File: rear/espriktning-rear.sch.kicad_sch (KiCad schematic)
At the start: 26 parts, among them J1 USB_C_Receptacle_USB2.0, J4 Conn_01x08, SW1 Reset, SW2 Flash

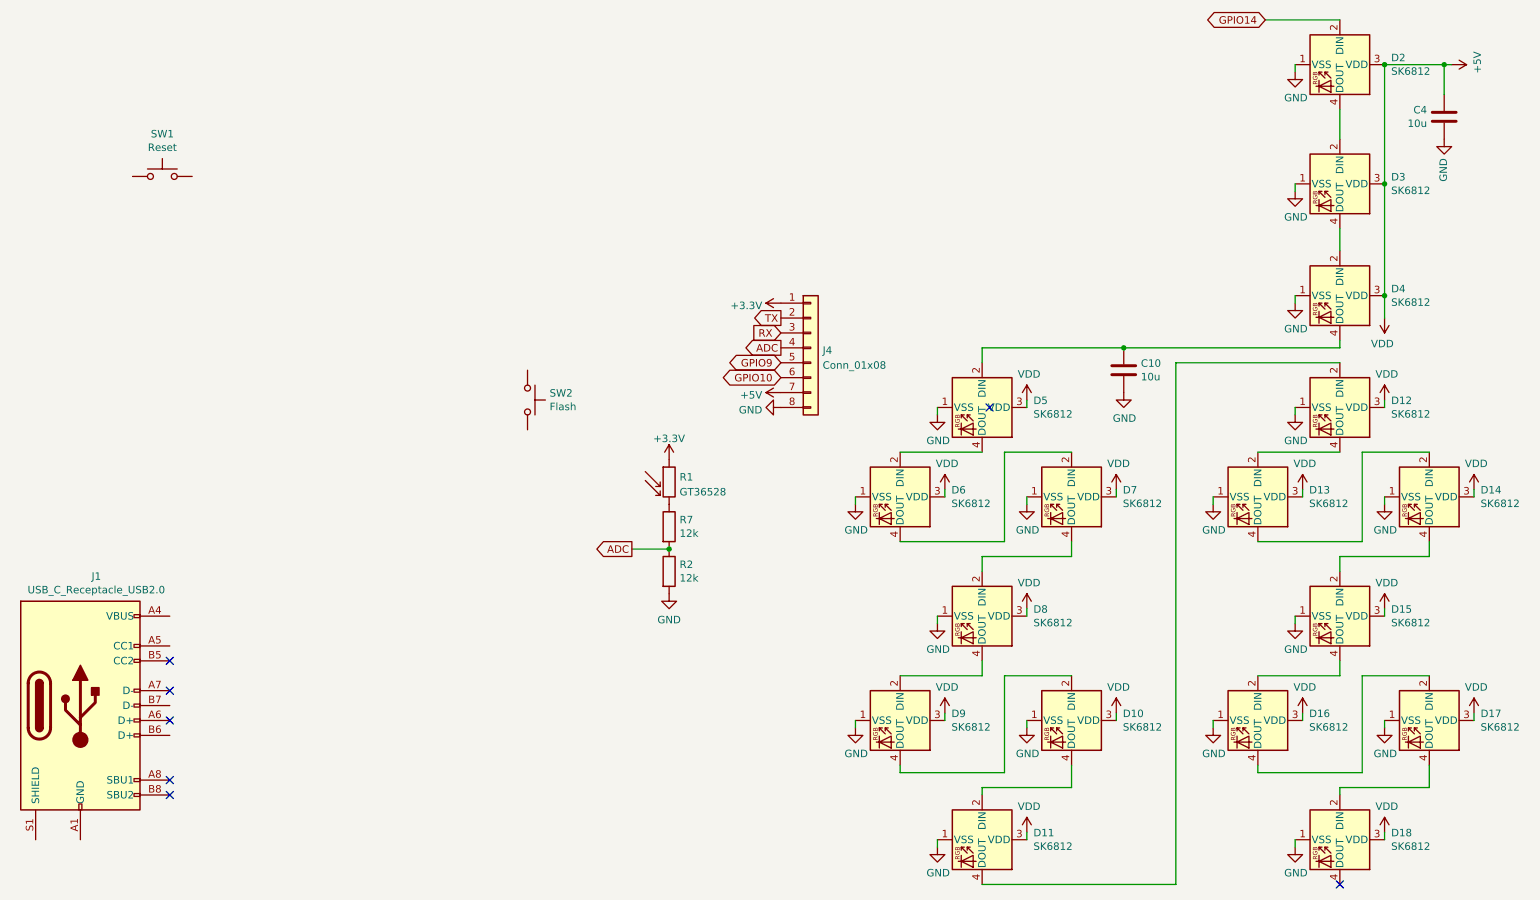
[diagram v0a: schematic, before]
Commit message: relayout to actually fit
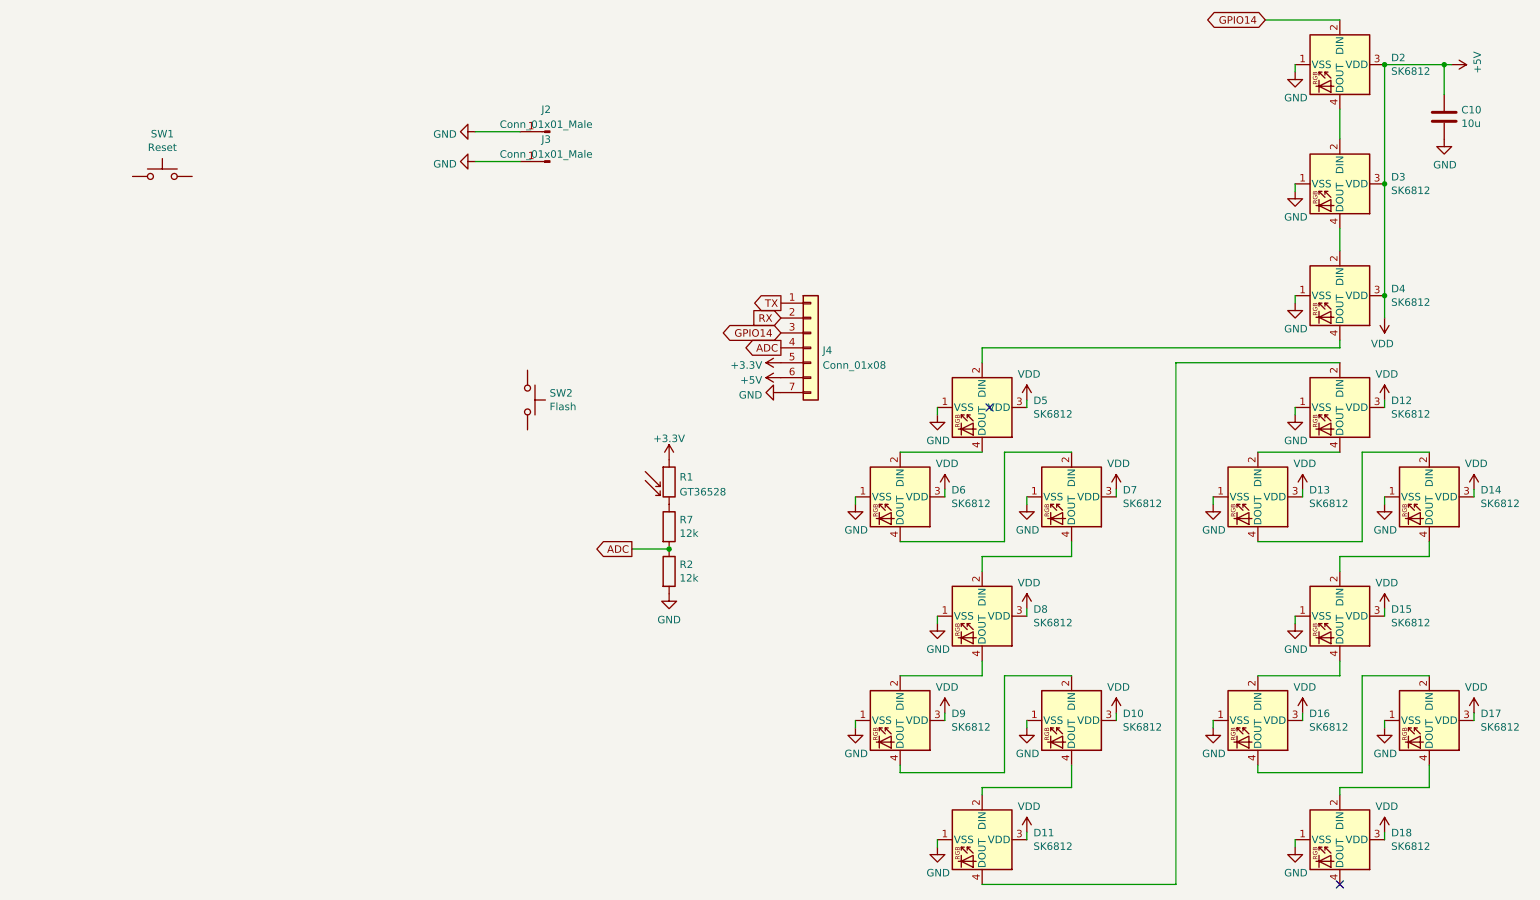
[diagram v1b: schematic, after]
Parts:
- removed C4: 10u, Capacitor_SMD:C_1206_3216Metric, symbol Device:C
- removed J1: USB_C_Receptacle_USB2.0, espriktning:usb-c-vertical-8, symbol Connector:USB_C_Receptacle_USB2.0
- added J2, J3: Conn_01x01_Male, Connector_Pin:Pin_D0.7mm_L6.5mm_W1.8mm_FlatFork, symbol Connector:Conn_01x01_Male
- J4: footprint Connector_PinSocket_1.00mm:PinSocket_1x08_P1.00mm_Vertical -> Connector_PinSocket_1.27mm:PinSocket_1x07_P1.27mm_Vertical; symbol Connector_Generic:Conn_01x08 -> Connector_Generic:Conn_01x07
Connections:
- net GPIO10 is gone; now on net +5V: J4.6 (Pin_6)
- net GPIO9 is gone; now on net +3V3: J4.5 (Pin_5)
- net +3V3: no longer J4.1 (Pin_1)
- net +5V: now also C10.1; no longer J4.7 (Pin_7)
- net GND: now also J4.7 (Pin_7), J2.1 (Pin_1), J3.1 (Pin_1); no longer J4.8 (Pin_8)
- net GPIO14: now also J4.3 (Pin_3)
- net RX: now also J4.2 (Pin_2); no longer J4.3 (Pin_3)
- net TX: now also J4.1 (Pin_1); no longer J4.2 (Pin_2)
- net at D4.4 (DOUT), D5.2 (DIN): no longer C10.1
- no-connect marks 7 -> 2
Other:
- moved on the sheet: C10
